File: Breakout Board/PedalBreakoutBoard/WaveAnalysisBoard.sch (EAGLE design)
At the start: 52 parts, among them IC1 LD1117V, IC2 MCP6004P, U1 OPA1652AID

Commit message: DP-97 - Add header component
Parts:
- added DIGILENT: SSQ-115-02-T-D-RA, SamacSys_Parts:SSQ-115-02-T-D-RA
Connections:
- new net AGND: AUD_GND.1, AUD_GND.2, C5.2, C7.2, IC2B.+IN, IC2D.+IN, IC2P.V-, R10.1, R2.1, R4.1, R8.1, SEED.AGND, U1.INB+, U1.V-
- net GND: no longer AUD_GND.1, AUD_GND.2, C5.2, C7.2, IC2B.+IN, IC2D.+IN, IC2P.V-, R10.1, R2.1, R4.1, R8.1, SEED.AGND, U1.INB+, U1.V-
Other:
- moved on the sheet: H5, H6, H7, H8

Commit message: DP-97 - Working on adding header
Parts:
- added J1, J2: NYS2152, SamacSys_Parts:NYS2152
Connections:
- new net N$11: DIGILENT.21
- new net N$16: DIGILENT.22
- new net N$17: DIGILENT.28
- new net N$19: DIGILENT.30
- new net N$20: DIGILENT.27
- new net N$21: DIGILENT.29
- net GND: now also DIGILENT.19, DIGILENT.20, DIGILENT.25, DIGILENT.26
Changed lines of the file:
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@@
 <schematic_group name="AUDIO_INPUT"/>
 <schematic_group name="AUDIO_PWR"/>
-<schematic_group name="AUDIO_JACKS"/>
 </groups>
 <parts>
@@
 <part name="SUPPLY6" library="supply2" library_urn="urn:adsk.eagle:library:372" deviceset="GND" device=""/>
 <part name="DIGILENT" library="SamacSys_Parts" deviceset="SSQ-115-02-T-D-RA" device=""/>
+<part name="SUPPLY7" library="supply2" library_urn="urn:adsk.eagle:library:372" deviceset="GND" device=""/>
+<part name="SUPPLY8" library="supply2" library_urn="urn:adsk.eagle:library:372" deviceset="GND" device=""/>
+<part name="J1" library="SamacSys_Parts" deviceset="NYS2152" device=""/>
+<part name="J2" library="SamacSys_Parts" deviceset="NYS2152" device=""/>
 </parts>
 <sheets>
@@
 <description>Audio &amp; Power</description>
 <plain>
-<text x="-20.32" y="157.48" size="1.778" layer="94" grouprefs="AUDIO_JACKS">Through-hole connectors wired out to 2 mono-TS jacks</text>
+<text x="-20.32" y="157.48" size="1.778" layer="94">Through-hole connectors wired out to 2 mono-TS jacks</text>
 <text x="7.62" y="25.4" size="1.778" layer="94" grouprefs="POWER">This section provides connection to a 9V
 barrel jack, feeding the V_IN pin on the Seed
@@
 <attribute name="VALUE" x="246.38" y="110.744" size="1.778" layer="96" font="vector" rot="R180" align="top-center"/>
 </instance>
-<instance part="AUD_PIN" gate="G$1" x="12.7" y="147.32" smashed="yes" grouprefs="AUDIO_JACKS">
+<instance part="AUD_PIN" gate="G$1" x="12.7" y="147.32" smashed="yes">
 <attribute name="VALUE" x="10.16" y="142.494" size="1.778" layer="96" font="vector"/>
 <attribute name="NAME" x="10.16" y="152.908" size="1.778" layer="95" font="vector"/>
 </instance>
-<instance part="AUD_GND" gate="G$1" x="2.54" y="149.86" smashed="yes" rot="R180" grouprefs="AUDIO_JACKS">
+<instance part="AUD_GND" gate="G$1" x="2.54" y="149.86" smashed="yes" rot="R180">
 <attribute name="VALUE" x="5.08" y="154.686" size="1.778" layer="96" font="vector" rot="R180"/>
 <attribute name="NAME" x="5.08" y="154.432" size="1.778" layer="95" font="vector" rot="R180"/>
@@
 <attribute name="VALUE" x="71.12" y="60.706" size="1.778" layer="96" align="top-center"/>
 </instance>
-<instance part="U$2" gate="G$1" x="-7.62" y="142.24" smashed="yes" grouprefs="AUDIO_JACKS">
+<instance part="U$2" gate="G$1" x="-7.62" y="142.24" smashed="yes">
 <attribute name="VALUE" x="-7.62" y="141.986" size="1.778" layer="96" align="top-center"/>
 </instance>
@@
 </instance>
 <instance part="DIGILENT" gate="G$1" x="-15.24" y="106.68" smashed="yes">
-<attribute name="NAME" x="3.81" y="114.3" size="1.778" layer="95" align="center-left"/>
-<attribute name="VALUE" x="3.81" y="111.76" size="1.778" layer="96" align="center-left"/>
+<attribute name="NAME" x="-13.97" y="114.3" size="1.778" layer="95" align="center-left"/>
+<attribute name="VALUE" x="-13.97" y="111.76" size="1.778" layer="96" align="center-left"/>
+</instance>
+<instance part="SUPPLY7" gate="GND" x="22.86" y="71.12" smashed="yes">
+<attribute name="VALUE" x="20.955" y="67.945" size="1.778" layer="96"/>
+</instance>
+<instance part="SUPPLY8" gate="GND" x="-33.02" y="71.12" smashed="yes">
+<attribute name="VALUE" x="-34.925" y="67.945" size="1.778" layer="96"/>
+</instance>
+<instance part="J1" gate="G$1" x="10.16" y="134.62" smashed="yes">
+<attribute name="NAME" x="26.67" y="142.24" size="1.778" layer="95" align="center-left"/>
+<attribute name="VALUE" x="26.67" y="139.7" size="1.778" layer="96" align="center-left"/>
+</instance>
+<instance part="J2" gate="G$1" x="-25.4" y="134.62" smashed="yes">
+<attribute name="NAME" x="-8.89" y="142.24" size="1.778" layer="95" align="center-left"/>
+<attribute name="VALUE" x="-8.89" y="139.7" size="1.778" layer="96" align="center-left"/>
 </instance>
 </instances>
@@
 <pinref part="C6" gate="G$1" pin="2"/>
 </segment>
+<segment>
+<pinref part="DIGILENT" gate="G$1" pin="20"/>
+<wire x1="7.62" y1="83.82" x2="17.78" y2="83.82" width="0.1524" layer="91"/>
+<pinref part="DIGILENT" gate="G$1" pin="26"/>
+<wire x1="7.62" y1="76.2" x2="17.78" y2="76.2" width="0.1524" layer="91"/>
+<wire x1="17.78" y1="83.82" x2="17.78" y2="76.2" width="0.1524" layer="91"/>
+<junction x="17.78" y="76.2"/>
+<wire x1="17.78" y1="76.2" x2="22.86" y2="76.2" width="0.1524" layer="91"/>
+<wire x1="22.86" y1="76.2" x2="22.86" y2="73.66" width="0.1524" layer="91"/>
+<pinref part="SUPPLY7" gate="GND" pin="GND"/>
+</segment>
+<segment>
+<pinref part="DIGILENT" gate="G$1" pin="19"/>
+<wire x1="-15.24" y1="83.82" x2="-27.94" y2="83.82" width="0.1524" layer="91"/>
+<wire x1="-27.94" y1="83.82" x2="-27.94" y2="76.2" width="0.1524" layer="91"/>
+<pinref part="DIGILENT" gate="G$1" pin="25"/>
+<wire x1="-27.94" y1="76.2" x2="-15.24" y2="76.2" width="0.1524" layer="91"/>
+<wire x1="-27.94" y1="76.2" x2="-33.02" y2="76.2" width="0.1524" layer="91"/>
+<junction x="-27.94" y="76.2"/>
+<wire x1="-33.02" y1="76.2" x2="-33.02" y2="73.66" width="0.1524" layer="91"/>
+<pinref part="SUPPLY8" gate="GND" pin="GND"/>
+</segment>
 </net>
 <net name="SPST1" class="0">
@@
 <net name="IN_L_JACK" class="0">
 <segment>
-<wire x1="20.32" y1="149.86" x2="27.94" y2="149.86" width="0.1524" layer="91" grouprefs="AUDIO_JACKS"/>
-<label x="22.86" y="149.86" size="1.778" layer="95" grouprefs="AUDIO_JACKS"/>
+<wire x1="20.32" y1="149.86" x2="27.94" y2="149.86" width="0.1524" layer="91"/>
+<label x="22.86" y="149.86" size="1.778" layer="95"/>
 <pinref part="AUD_PIN" gate="G$1" pin="2"/>
 </segment>
@@
 <net name="OUT_L_JACK" class="0">
 <segment>
-<wire x1="20.32" y1="147.32" x2="27.94" y2="147.32" width="0.1524" layer="91" grouprefs="AUDIO_JACKS"/>
-<label x="22.86" y="147.32" size="1.778" layer="95" grouprefs="AUDIO_JACKS"/>
+<wire x1="20.32" y1="147.32" x2="27.94" y2="147.32" width="0.1524" layer="91"/>
+<label x="22.86" y="147.32" size="1.778" layer="95"/>
 <pinref part="AUD_PIN" gate="G$1" pin="1"/>
 </segment>
@@
 <segment>
 <pinref part="AUD_GND" gate="G$1" pin="1"/>
-<wire x1="-5.08" y1="149.86" x2="-7.62" y2="149.86" width="0.1524" layer="91" grouprefs="AUDIO_JACKS"/>
-<wire x1="-7.62" y1="149.86" x2="-7.62" y2="147.32" width="0.1524" layer="91" grouprefs="AUDIO_JACKS"/>
+<wire x1="-5.08" y1="149.86" x2="-7.62" y2="149.86" width="0.1524" layer="91"/>
+<wire x1="-7.62" y1="149.86" x2="-7.62" y2="147.32" width="0.1524" layer="91"/>
 <pinref part="AUD_GND" gate="G$1" pin="2"/>
-<wire x1="-7.62" y1="147.32" x2="-7.62" y2="144.78" width="0.1524" layer="91" grouprefs="AUDIO_JACKS"/>
-<wire x1="-5.08" y1="147.32" x2="-7.62" y2="147.32" width="0.1524" layer="91" grouprefs="AUDIO_JACKS"/>
-<junction x="-7.62" y="147.32" grouprefs="AUDIO_JACKS"/>
+<wire x1="-7.62" y1="147.32" x2="-7.62" y2="144.78" width="0.1524" layer="91"/>
+<wire x1="-5.08" y1="147.32" x2="-7.62" y2="147.32" width="0.1524" layer="91"/>
+<junction x="-7.62" y="147.32"/>
 <pinref part="U$2" gate="G$1" pin="AGND"/>
 </segment>
@@
 </segment>
 </net>
+<net name="N$11" class="0">
+<segment>
+<pinref part="DIGILENT" gate="G$1" pin="21"/>
+<wire x1="-15.24" y1="81.28" x2="-22.86" y2="81.28" width="0.1524" layer="91"/>
+</segment>
+</net>
+<net name="N$16" class="0">
+<segment>
+<pinref part="DIGILENT" gate="G$1" pin="22"/>
+<wire x1="7.62" y1="81.28" x2="15.24" y2="81.28" width="0.1524" layer="91"/>
+</segment>
+</net>
+<net name="N$17" class="0">
+<segment>
+<pinref part="DIGILENT" gate="G$1" pin="28"/>
+<wire x1="7.62" y1="73.66" x2="15.24" y2="73.66" width="0.1524" layer="91"/>
+</segment>
+</net>
+<net name="N$19" class="0">
+<segment>
+<pinref part="DIGILENT" gate="G$1" pin="30"/>
+<wire x1="7.62" y1="71.12" x2="15.24" y2="71.12" width="0.1524" layer="91"/>
+</segment>
+</net>
+<net name="N$20" class="0">
+<segment>
+<pinref part="DIGILENT" gate="G$1" pin="27"/>
+<wire x1="-15.24" y1="73.66" x2="-22.86" y2="73.66" width="0.1524" layer="91"/>
+</segment>
+</net>
+<net name="N$21" class="0">
+<segment>
+<pinref part="DIGILENT" gate="G$1" pin="29"/>
+<wire x1="-15.24" y1="71.12" x2="-22.86" y2="71.12" width="0.1524" layer="91"/>
+</segment>
+</net>

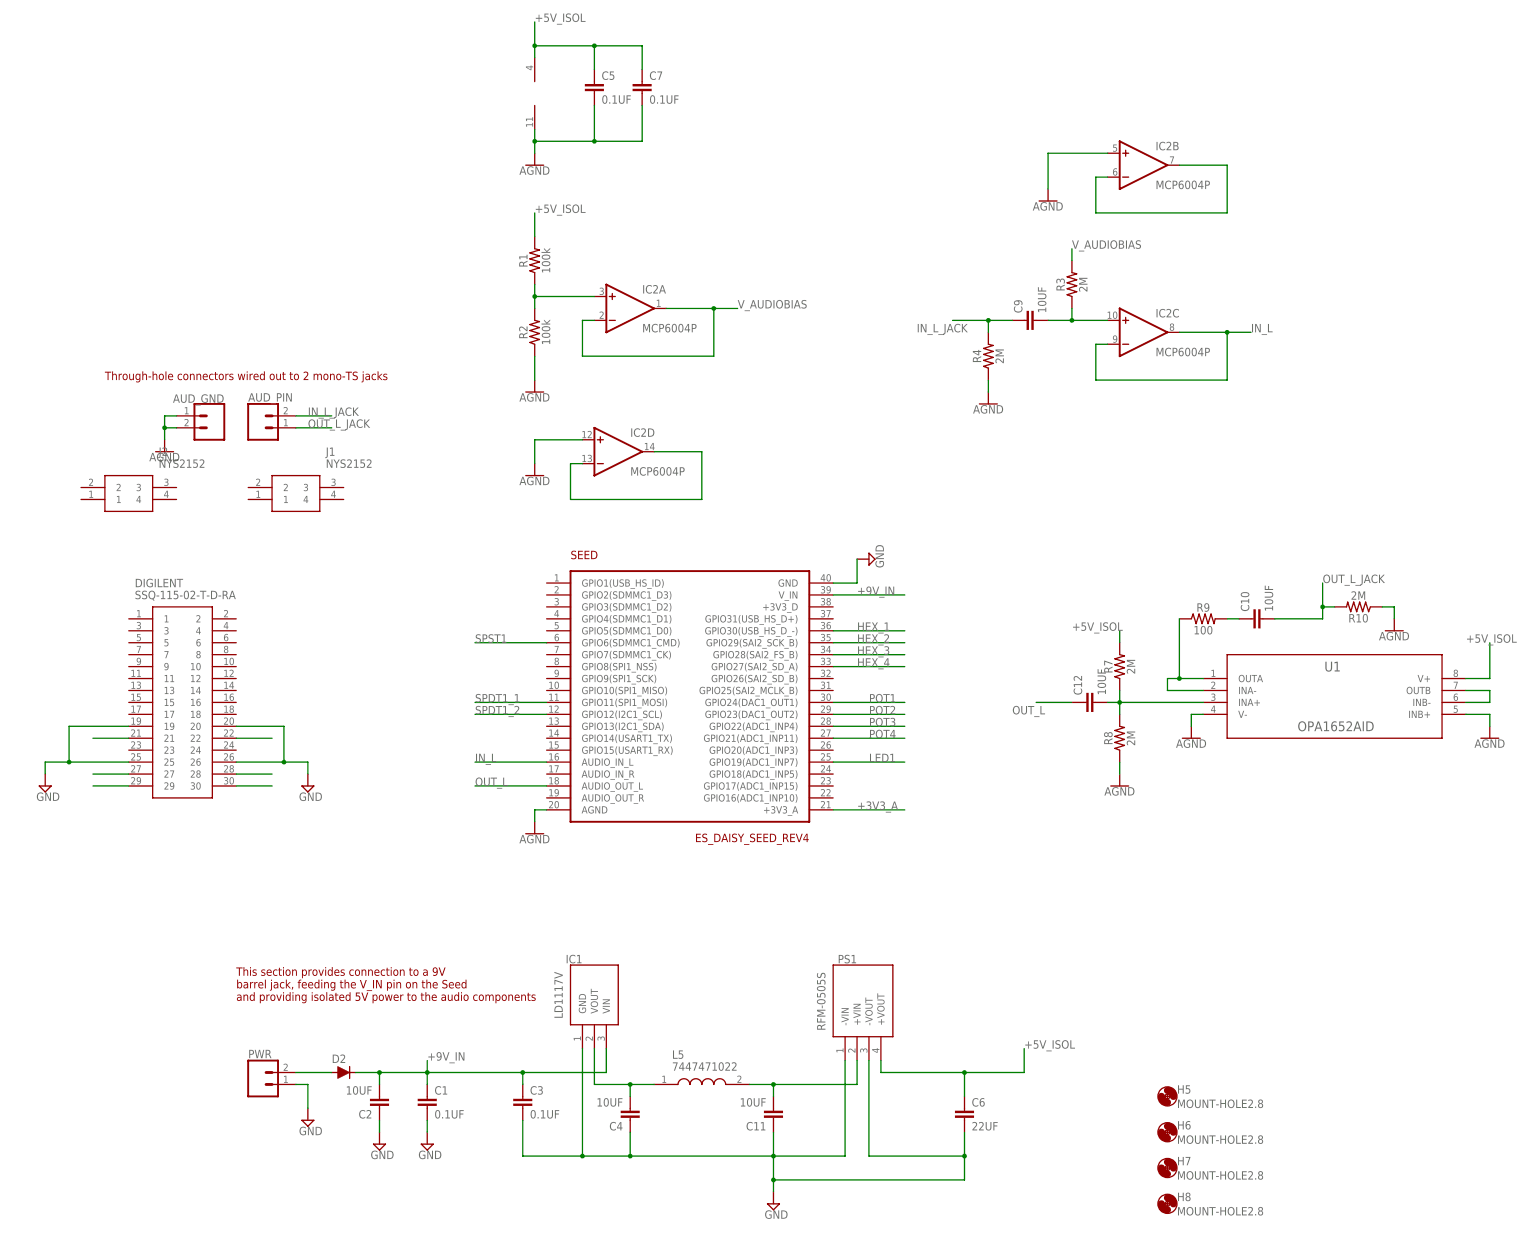
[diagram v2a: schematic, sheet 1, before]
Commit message: DP-97 - Update multi-effect with new grounding scheme
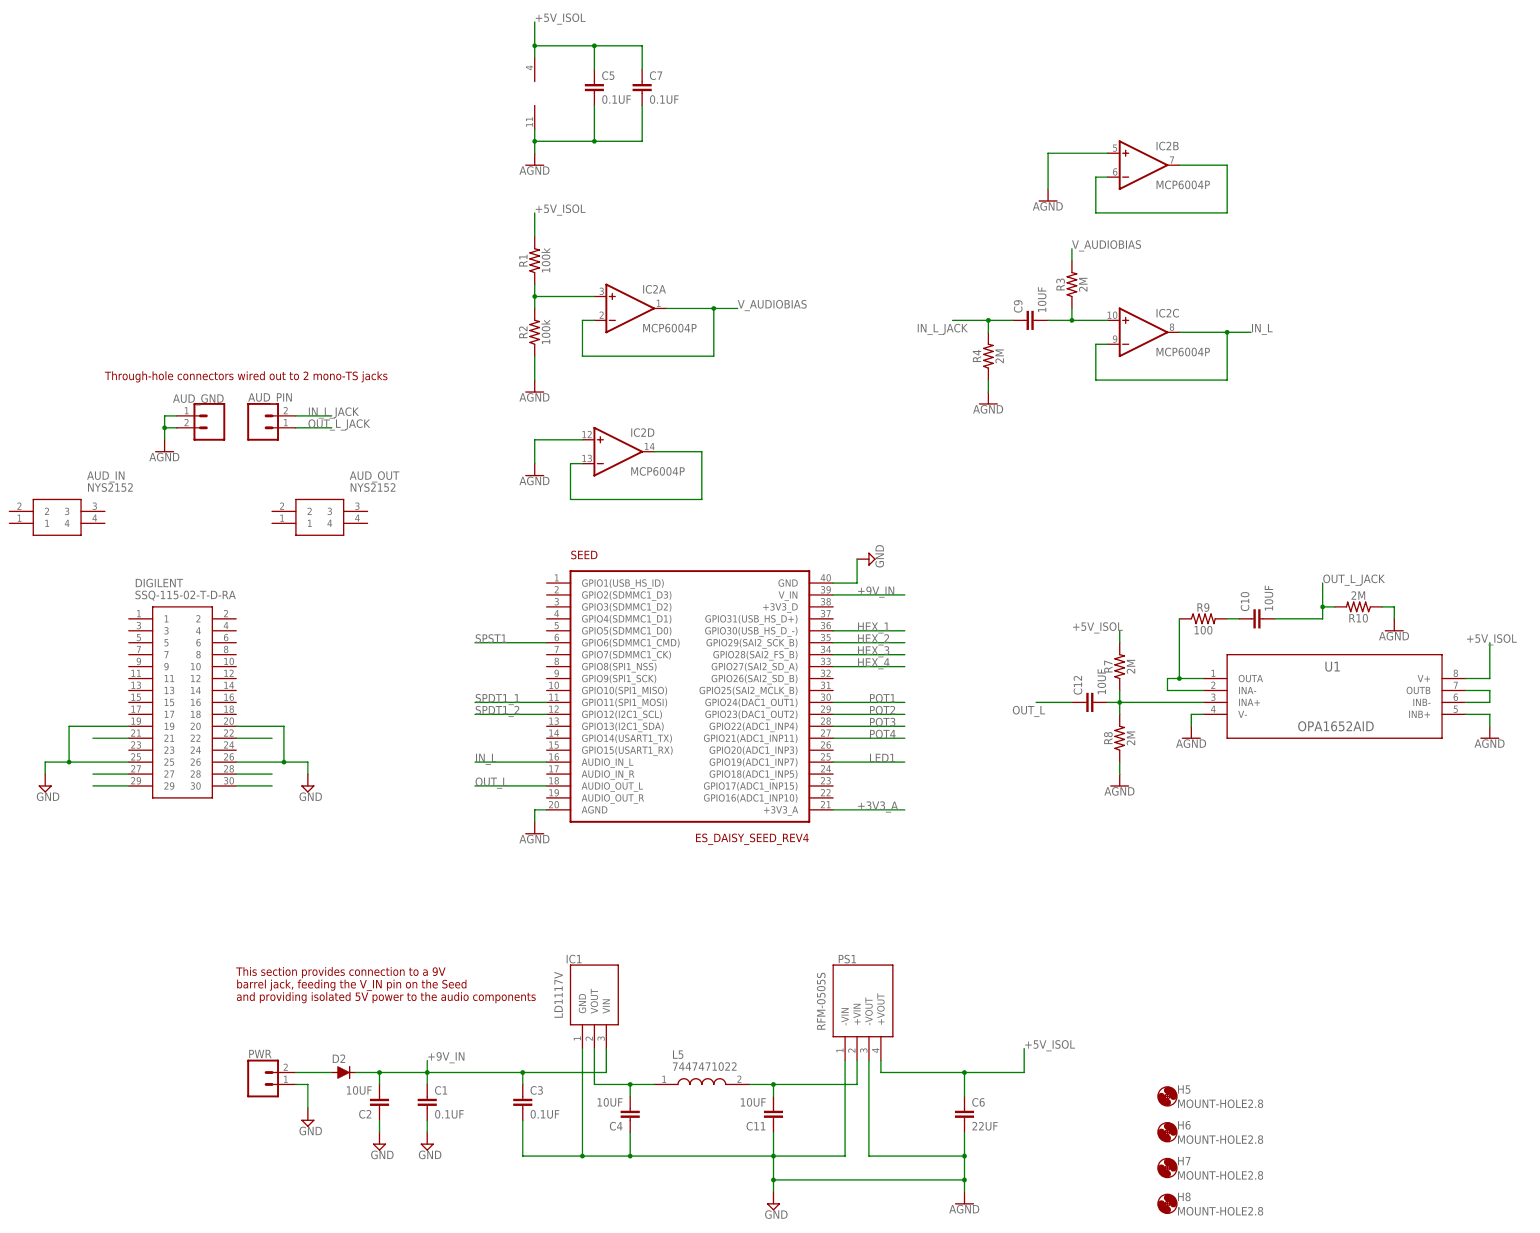
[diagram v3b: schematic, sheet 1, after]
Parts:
- removed J1, J2: NYS2152, SamacSys_Parts:NYS2152
- added AUD_IN, AUD_OUT: NYS2152, SamacSys_Parts:NYS2152
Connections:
- net AGND: now also C11.1, C3.2, C4.1, C6.2, IC1.GND, PS1.-VIN, PS1.-VOUT
- net GND: no longer C11.1, C3.2, C4.1, C6.2, IC1.GND, PS1.-VIN, PS1.-VOUT
